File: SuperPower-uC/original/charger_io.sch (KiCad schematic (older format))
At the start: 20 parts, among them J2 Barrel_Jack_Switch, J3 Conn_01x02_Male, Q2 DMP3028LSD, U2 USB-C, U3 IP4220CZ6

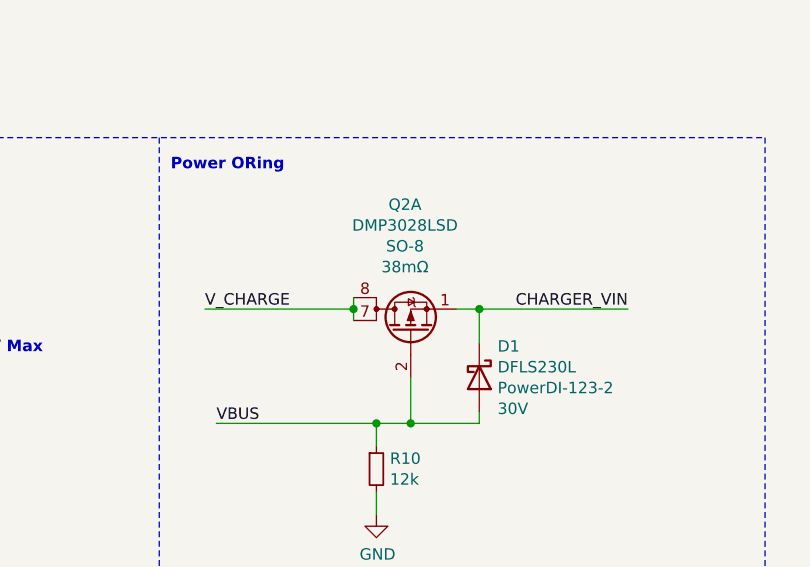
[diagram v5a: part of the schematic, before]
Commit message: Exchanged DMP3028LSD mosfet with Si3421DV
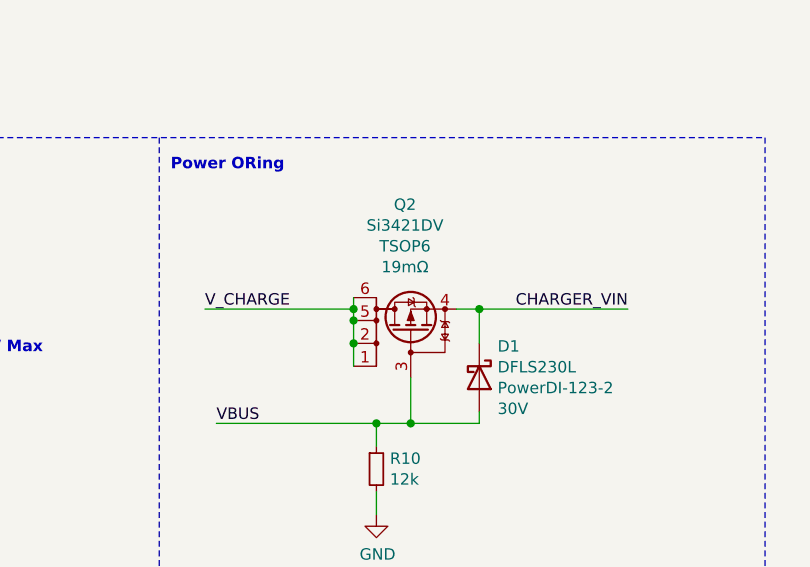
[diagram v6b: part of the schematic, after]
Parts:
- removed Q2: DMP3028LSD, Package_SO:SO-8_3.9x4.9mm_P1.27mm, symbol dmp3028lsd:DMP3028LSD
- added Q2: Si3421DV, Package_SO:TSOP-6_1.65x3.05mm_P0.95mm, symbol dmp2035uvt:DMP2035UVT
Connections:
- net CHARGER_VIN: now also Q2.4 (S)
- net VBUS: now also Q2.3 (G)
- net V_CHARGE: now also Q2.1 (D), Q2.2 (D), Q2.5 (D), Q2.6 (D)
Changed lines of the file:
@@
 Wire Wire Line
 	8600 2850 9250 2850
-$Comp
-L dmp3028lsd:DMP3028LSD Q2
-U 1 1 6007EF0E
-P 9500 2950
-F 0 "Q2" V 10057 2975 50  0000 C CNN
-F 1 "DMP3028LSD" V 9966 2975 50  0000 C CNN
-F 2 "Package_SO:SO-8_3.9x4.9mm_P1.27mm" H 9700 2875 50  0001 L CIN
-F 3 "https://www.diodes.com/assets/Datasheets/DMP3028LSD.pdf" V 9500 2950 50  0001 L CNN
-F 4 "Diodes Incorporated" H 9500 2950 50  0001 C CNN "Mfr_name"
-F 5 "DMP3028LSD-13" H 9500 2950 50  0001 C CNN "Mfr_no"
-F 6 "SO-8" V 9875 2975 50  0000 C CNN "Package"
-F 7 "P + P" H 9500 2950 50  0001 C CNN "mos_Type"
-F 8 "30V" H 9500 2950 50  0001 C CNN "mos_VDSS"
-F 9 "38mΩ" V 9784 2975 50  0000 C CNN "mos_RDSon"
-F 10 "4.7A" H 9500 2950 50  0001 C CNN "mos_IDmax"
-F 11 "1-3V" H 9500 2950 50  0001 C CNN "mos_VGSth"
-F 12 "20V" H 9500 2950 50  0001 C CNN "mos_VGSS"
-F 13 "https://octopart.com/dmp3028lsd-13-diodes+inc.-67250487?r=sp" H 9500 2950 50  0001 C CNN "Octopart_link"
-F 14 "-" H 9500 2950 50  0001 C CNN "Farnell_link"
-F 15 "-" H 9500 2950 50  0001 C CNN "Farnell_ref"
-F 16 "2020-12-05" H 9500 2950 50  0001 C CNN "Farnell_check_date"
-F 17 "-" H 9500 2950 50  0001 C CNN "Farnell_price_qt=1"
-F 18 "-" H 9500 2950 50  0001 C CNN "Farnell_price_qt=10"
-F 19 "-" H 9500 2950 50  0001 C CNN "Farnell_price_qt=100"
-F 20 "-" H 9500 2950 50  0001 C CNN "Farnell_price_qt=1000"
-F 21 "-" H 9500 2950 50  0001 C CNN "Farnell_stock"
-F 22 "https://lcsc.com/product-detail/MOSFET_Diodes-Incorporated-DMP3028LSD-13_C397949.html" H 9500 2950 50  0001 C CNN "LCSC_link"
-F 23 "C397949" H 9500 2950 50  0001 C CNN "LCSC_ref"
-F 24 "2020-12-13" H 9500 2950 50  0001 C CNN "LCSC_check_date"
-F 25 "$0.373" H 9500 2950 50  0001 C CNN "LCSC_price_qt=1"
-F 26 "$0.2802" H 9500 2950 50  0001 C CNN "LCSC_price_qt=10"
-F 27 "$0.2475" H 9500 2950 50  0001 C CNN "LCSC_price_qt=100"
-F 28 "$0.2355" H 9500 2950 50  0001 C CNN "LCSC_price_qt=1000"
-F 29 "4,818" H 9500 2950 50  0001 C CNN "LCSC_stock"
-F 30 "https://www.mouser.fr/ProductDetail/Diodes-Incorporated/DMP3028LSD-13?qs=%2Fha2pyFadugUkRnXWzNfjPB%2F2%2FpUVmcBtenJqlz85NswHo6v693iIw%3D%3D" H 9500 2950 50  0001 C CNN "Mouser_link"
-F 31 "621-DMP3028LSD-13" H 9500 2950 50  0001 C CNN "Mouser_ref"
-F 32 "2020-12-13" H 9500 2950 50  0001 C CNN "Mouser_check_date"
-F 33 "$0.564" H 9500 2950 50  0001 C CNN "Mouser_price_qt=1"
-F 34 "$0.469" H 9500 2950 50  0001 C CNN "Mouser_price_qt=10"
-F 35 "$0.328" H 9500 2950 50  0001 C CNN "Mouser_price_qt=100"
-F 36 "$0.242" H 9500 2950 50  0001 C CNN "Mouser_price_qt=1000"
-F 37 "2,855" H 9500 2950 50  0001 C CNN "Mouser_stock"
-F 38 "-" H 9500 2950 50  0001 C CNN "RS_link"
-F 39 "-" H 9500 2950 50  0001 C CNN "RS_ref"
-F 40 "2020-12-05" H 9500 2950 50  0001 C CNN "RS_check_date"
-F 41 "-" H 9500 2950 50  0001 C CNN "RS_price_qt=1"
-F 42 "-" H 9500 2950 50  0001 C CNN "RS_price_qt=10"
-F 43 "-" H 9500 2950 50  0001 C CNN "RS_price_qt=100"
-F 44 "-" H 9500 2950 50  0001 C CNN "RS_price_qt=1000"
-F 45 "-" H 9500 2950 50  0001 C CNN "RS_stock"
-F 46 "TO_CHECK" H 9500 2950 50  0001 C CNN "Status"
-F 47 "1.03" H 9500 2950 50  0001 C CNN "Release_version"
-F 48 "2020-12-21" H 9500 2950 50  0001 C CNN "Release_date"
-F 49 "ManWithNoName" H 9500 2950 50  0001 C CNN "Designer"
-	1    9500 2950
-	0    -1   -1   0
-$EndComp
 Wire Wire Line
 	8650 3350 9350 3350
@@
 Wire Wire Line
 	9250 2850 9250 2800
+$Comp
+L dmp2035uvt:DMP2035UVT Q?
+U 1 1 6007A550
+P 9500 2950
+AR Path="/5F63A0E9/6007A550" Ref="Q?"  Part="1"
+AR Path="/5F63B107/6007A550" Ref="Q2"  Part="1"
+F 0 "Q2" V 10057 2975 50  0000 C CNN
+F 1 "Si3421DV" V 9966 2975 50  0000 C CNN
+F 2 "Package_SO:TSOP-6_1.65x3.05mm_P0.95mm" H 9700 3050 50  0001 C CNN
+F 3 "https://www.diodes.com/assets/Datasheets/DMP2035UVT.pdf" H 9500 2950 50  0001 C CNN
+F 4 "Diodes Incorporated" H 9500 2950 50  0001 C CNN "Mfr_name"
+F 5 "DMP2035UVT-7" H 9500 2950 50  0001 C CNN "Mfr_no"
+F 6 "TSOP6" V 9875 2975 50  0000 C CNN "Package"
+F 7 "P" H 9500 2950 50  0001 C CNN "mos_Type"
+F 8 "-20V" H 9500 2950 50  0001 C CNN "mos_VDSS"
+F 9 "19mΩ" V 9784 2975 50  0000 C CNN "mos_RDSon"
+F 10 "-6.0A" H 9500 2950 50  0001 C CNN "mos_IDmax"
+F 11 "-0.4V_to_-1.5V" H 9500 2950 50  0001 C CNN "mos_VGSth"
+F 12 "12V" H 9500 2950 50  0001 C CNN "mos_VGSS"
+F 13 "https://octopart.com/dmp2035uvt-7-diodes+inc.-21789379?r=sp" H 9500 2950 50  0001 C CNN "Octopart_link"
+F 14 "https://fr.farnell.com/diodes-inc/dmp2035uvt-7/mosfet-canal-p-20v-6a-150-1-2w/dp/3405183?st=dmp2035uvt" H 9500 2950 50  0001 C CNN "Farnell_link"
+F 15 "3405183" H 9500 2950 50  0001 C CNN "Farnell_ref"
+F 16 "2020-12-11" H 9500 2950 50  0001 C CNN "Farnell_check_date"
+F 17 "-" H 9500 2950 50  0001 C CNN "Farnell_price_qt=1"
+F 18 "0,52 €" H 9500 2950 50  0001 C CNN "Farnell_price_qt=10"
+F 19 "0,238 €" H 9500 2950 50  0001 C CNN "Farnell_price_qt=100"
+F 20 "0,141 €" H 9500 2950 50  0001 C CNN "Farnell_price_qt=1000"
+F 21 "2,890" H 9500 2950 50  0001 C CNN "Farnell_stock"
+F 22 "https://lcsc.com/product-detail/MOSFET_Diodes-Incorporated-DMP2035UVT-7_C260934.html" H 9500 2950 50  0001 C CNN "LCSC_link"
+F 23 "C260934" H 9500 2950 50  0001 C CNN "LCSC_ref"
+F 24 "2020-12-11" H 9500 2950 50  0001 C CNN "LCSC_check_date"
+F 25 "-" H 9500 2950 50  0001 C CNN "LCSC_price_qt=1"
+F 26 "$0.1253" H 9500 2950 50  0001 C CNN "LCSC_price_qt=10"
+F 27 "$0.0932" H 9500 2950 50  0001 C CNN "LCSC_price_qt=100"
+F 28 "$0.0814" H 9500 2950 50  0001 C CNN "LCSC_price_qt=1000"
+F 29 "7,535" H 9500 2950 50  0001 C CNN "LCSC_stock"
+F 30 "https://eu.mouser.com/ProductDetail/Diodes-Incorporated/DMP2035UVT-7?qs=F5djdNSOT4Y3SEHDwWTQ6g%3D%3D" H 9500 2950 50  0001 C CNN "Mouser_link"
+F 31 "621-DMP2035UVT-7" H 9500 2950 50  0001 C CNN "Mouser_ref"
+F 32 "2020-12-11" H 9500 2950 50  0001 C CNN "Mouser_check_date"
+F 33 "$0.474" H 9500 2950 50  0001 C CNN "Mouser_price_qt=1"
+F 34 "$0.346" H 9500 2950 50  0001 C CNN "Mouser_price_qt=10"
+F 35 "$0.215" H 9500 2950 50  0001 C CNN "Mouser_price_qt=100"
+F 36 "$0.137" H 9500 2950 50  0001 C CNN "Mouser_price_qt=1000"
+F 37 "19,684" H 9500 2950 50  0001 C CNN "Mouser_stock"
+F 38 "-" H 9500 2950 50  0001 C CNN "RS_link"
+F 39 "-" H 9500 2950 50  0001 C CNN "RS_ref"
+F 40 "2020-12-11" H 9500 2950 50  0001 C CNN "RS_check_date"
+F 41 "-" H 9500 2950 50  0001 C CNN "RS_price_qt=1"
+F 42 "-" H 9500 2950 50  0001 C CNN "RS_price_qt=10"
+F 43 "-" H 9500 2950 50  0001 C CNN "RS_price_qt=100"
+F 44 "-" H 9500 2950 50  0001 C CNN "RS_price_qt=1000"
+F 45 "-" H 9500 2950 50  0001 C CNN "RS_stock"
+F 46 "TO_CHECK" H 9500 2950 50  0001 C CNN "Status"
+F 47 "1.01" H 9500 2950 50  0001 C CNN "Release_version"
+F 48 "2020-12-18" H 9500 2950 50  0001 C CNN "Release_date"
+F 49 "ManWithNoName" H 9500 2950 50  0001 C CNN "Designer"
+	1    9500 2950
+	0    -1   -1   0
+$EndComp
+Wire Wire Line
+	9250 3100 9250 3000
+Connection ~ 9250 2900
+Connection ~ 9250 3000
+Wire Wire Line
+	9250 3000 9250 2900
 $EndSCHEMATC

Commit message: Exchanged MH with 2.5 + Vias and Pad
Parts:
- H1, H2, H3, H4: footprint MountingHole:MountingHole_2.2mm_M2 -> MountingHole:MountingHole_2.5mm_Pad_Via
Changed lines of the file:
@@
 F 0 "H1" H 1450 2599 50  0000 L CNN
 F 1 "MountingHole_Pad" H 1450 2508 50  0000 L CNN
-F 2 "MountingHole:MountingHole_2.2mm_M2" H 1350 2550 50  0001 C CNN
+F 2 "MountingHole:MountingHole_2.5mm_Pad_Via" H 1350 2550 50  0001 C CNN
 F 3 "~" H 1350 2550 50  0001 C CNN
 	1    1350 2550
@@
 F 0 "H3" H 2350 2599 50  0000 L CNN
 F 1 "MountingHole_Pad" H 2350 2508 50  0000 L CNN
-F 2 "MountingHole:MountingHole_2.2mm_M2" H 2250 2550 50  0001 C CNN
+F 2 "MountingHole:MountingHole_2.5mm_Pad_Via" H 2250 2550 50  0001 C CNN
 F 3 "~" H 2250 2550 50  0001 C CNN
 	1    2250 2550
@@
 F 0 "H2" H 1450 3349 50  0000 L CNN
 F 1 "MountingHole_Pad" H 1450 3258 50  0000 L CNN
-F 2 "MountingHole:MountingHole_2.2mm_M2" H 1350 3300 50  0001 C CNN
+F 2 "MountingHole:MountingHole_2.5mm_Pad_Via" H 1350 3300 50  0001 C CNN
 F 3 "~" H 1350 3300 50  0001 C CNN
 	1    1350 3300
@@
 F 0 "H4" H 2350 3349 50  0000 L CNN
 F 1 "MountingHole_Pad" H 2350 3258 50  0000 L CNN
-F 2 "MountingHole:MountingHole_2.2mm_M2" H 2250 3300 50  0001 C CNN
+F 2 "MountingHole:MountingHole_2.5mm_Pad_Via" H 2250 3300 50  0001 C CNN
 F 3 "~" H 2250 3300 50  0001 C CNN
 	1    2250 3300

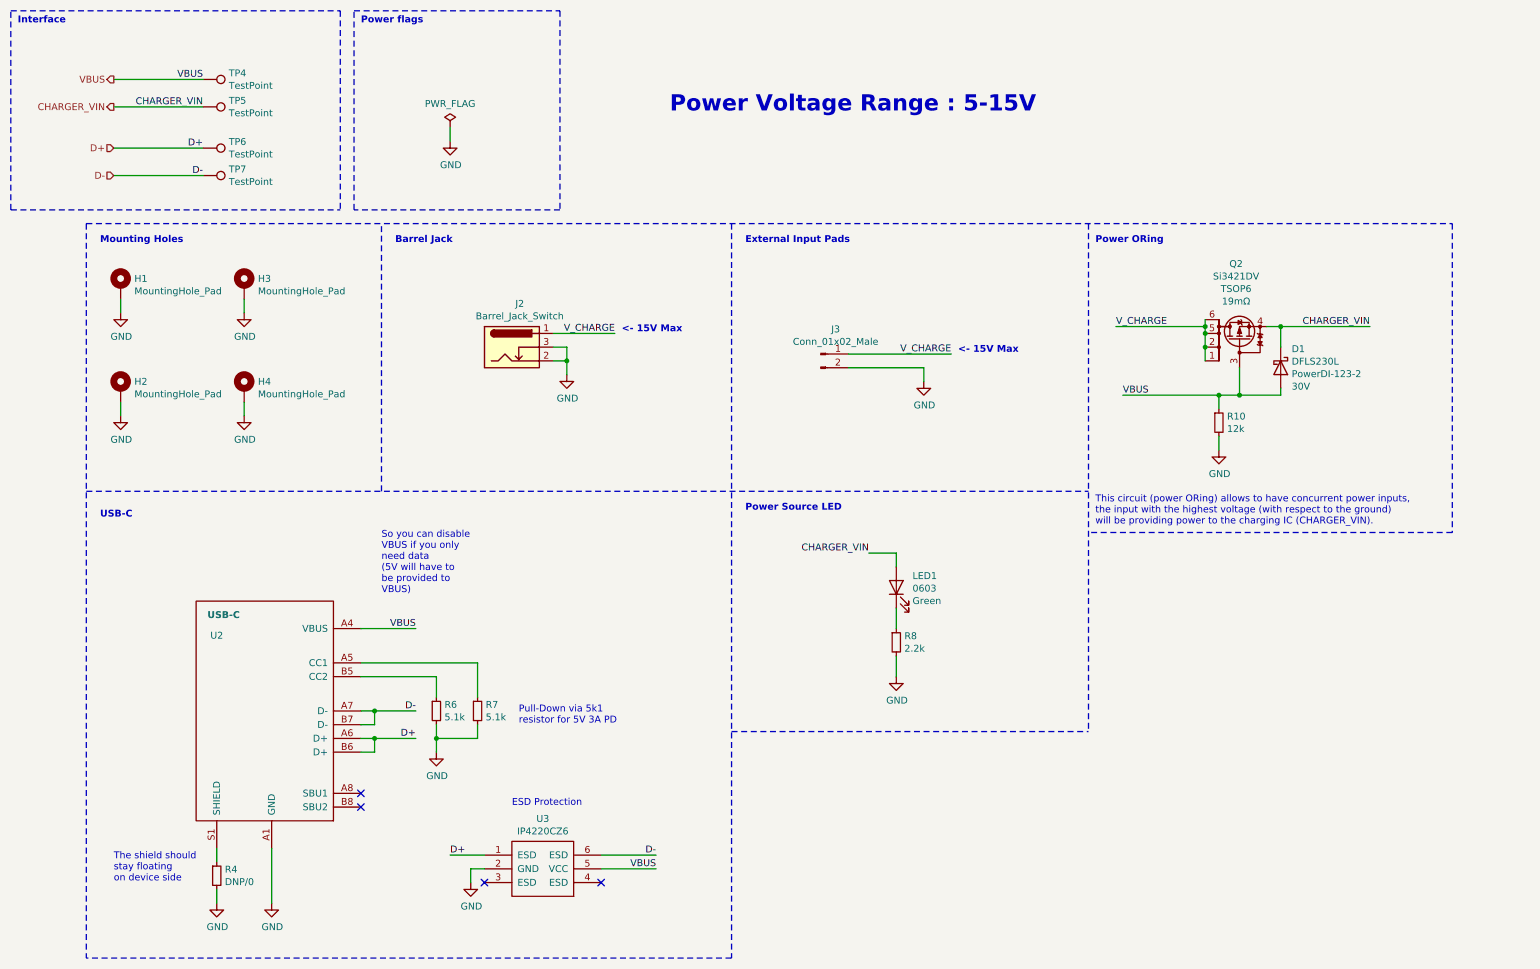
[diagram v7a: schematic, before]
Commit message: Swapped M2.5 with pad to M2.2 without pads
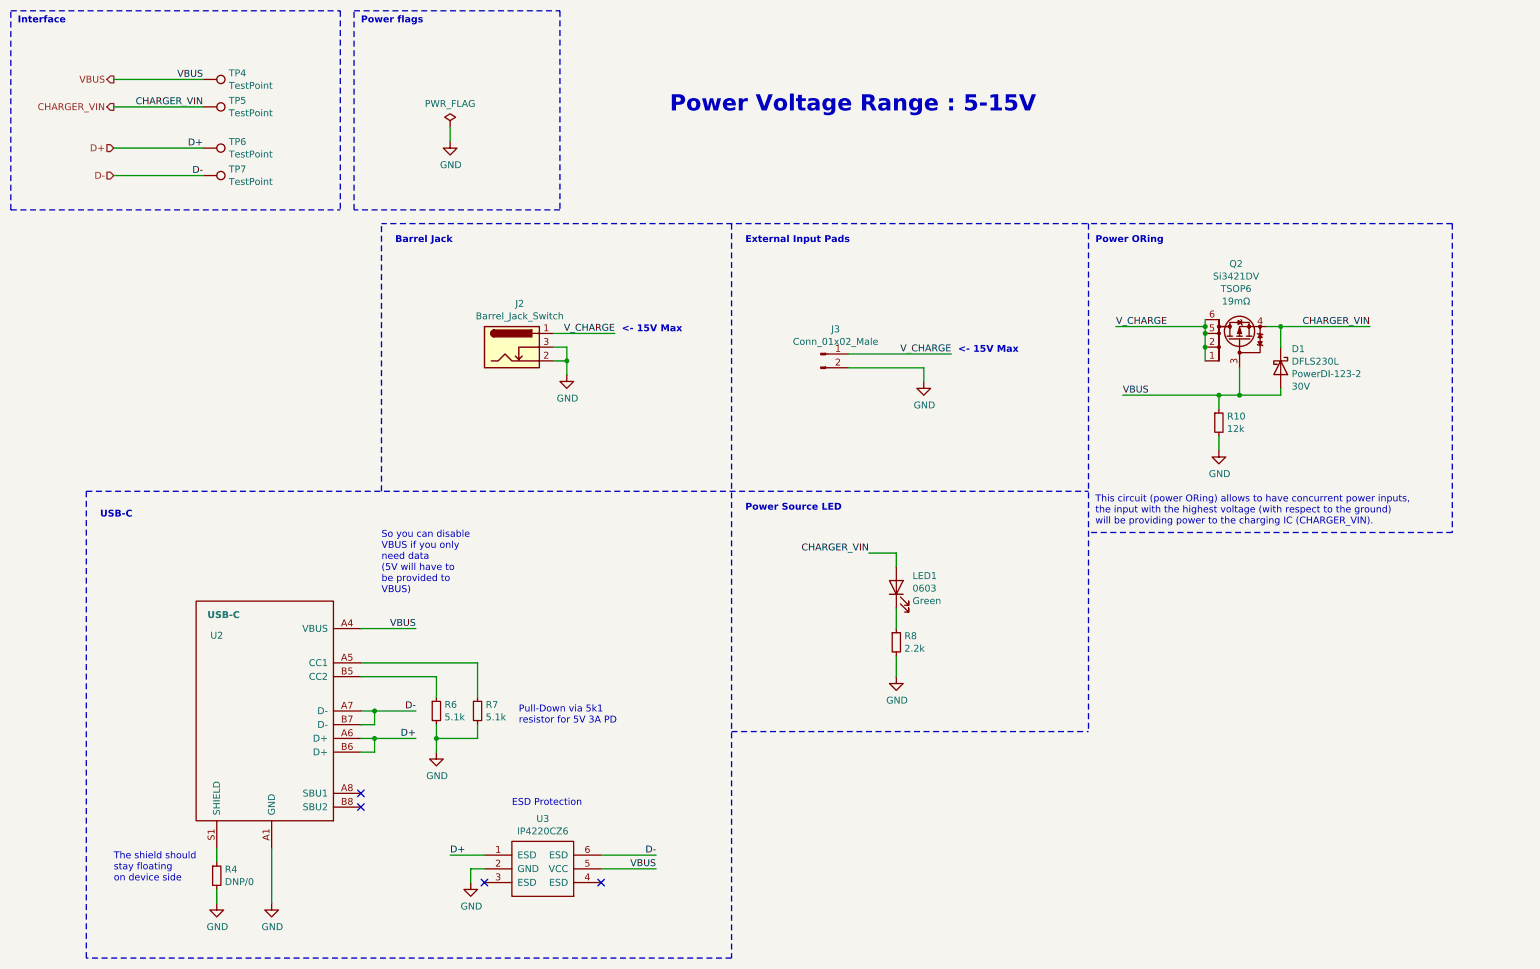
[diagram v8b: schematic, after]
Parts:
- removed H1, H2, H3, H4: MountingHole_Pad, MountingHole:MountingHole_2.5mm_Pad_Via, symbol Mechanical:MountingHole_Pad
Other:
- note removed: "Mounting Holes"
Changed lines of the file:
@@
 Text Notes 7450 3050 0    50   ~ 10
 <- 15V Max
-$Comp
-L Mechanical:MountingHole_Pad H1
-U 1 1 5FDDE91A
-P 1350 2550
-F 0 "H1" H 1450 2599 50  0000 L CNN
-F 1 "MountingHole_Pad" H 1450 2508 50  0000 L CNN
-F 2 "MountingHole:MountingHole_2.5mm_Pad_Via" H 1350 2550 50  0001 C CNN
-F 3 "~" H 1350 2550 50  0001 C CNN
-	1    1350 2550
-	1    0    0    -1
-$EndComp
-$Comp
-L power:GND #PWR010
-U 1 1 5FDE07B4
-P 1350 2750
-F 0 "#PWR010" H 1350 2500 50  0001 C CNN
-F 1 "GND" H 1355 2577 50  0000 C CNN
-F 2 "" H 1350 2750 50  0001 C CNN
-F 3 "" H 1350 2750 50  0001 C CNN
-	1    1350 2750
-	1    0    0    -1
-$EndComp
-Wire Wire Line
-	1350 2750 1350 2650
-Wire Notes Line
-	1100 2100 1100 7450
-Wire Notes Line
-	1100 2100 11050 2100
-Text Notes 1200 2250 0    50   ~ 10
-Mounting Holes
-$Comp
-L Mechanical:MountingHole_Pad H3
-U 1 1 5FDE96CE
-P 2250 2550
-F 0 "H3" H 2350 2599 50  0000 L CNN
-F 1 "MountingHole_Pad" H 2350 2508 50  0000 L CNN
-F 2 "MountingHole:MountingHole_2.5mm_Pad_Via" H 2250 2550 50  0001 C CNN
-F 3 "~" H 2250 2550 50  0001 C CNN
-	1    2250 2550
-	1    0    0    -1
-$EndComp
-$Comp
-L power:GND #PWR013
-U 1 1 5FDE96D4
-P 2250 2750
-F 0 "#PWR013" H 2250 2500 50  0001 C CNN
-F 1 "GND" H 2255 2577 50  0000 C CNN
-F 2 "" H 2250 2750 50  0001 C CNN
-F 3 "" H 2250 2750 50  0001 C CNN
-	1    2250 2750
-	1    0    0    -1
-$EndComp
-Wire Wire Line
-	2250 2750 2250 2650
-$Comp
-L Mechanical:MountingHole_Pad H2
-U 1 1 5FDEB8E4
-P 1350 3300
-F 0 "H2" H 1450 3349 50  0000 L CNN
-F 1 "MountingHole_Pad" H 1450 3258 50  0000 L CNN
-F 2 "MountingHole:MountingHole_2.5mm_Pad_Via" H 1350 3300 50  0001 C CNN
-F 3 "~" H 1350 3300 50  0001 C CNN
-	1    1350 3300
-	1    0    0    -1
-$EndComp
-$Comp
-L power:GND #PWR011
-U 1 1 5FDEB8EA
-P 1350 3500
-F 0 "#PWR011" H 1350 3250 50  0001 C CNN
-F 1 "GND" H 1355 3327 50  0000 C CNN
-F 2 "" H 1350 3500 50  0001 C CNN
-F 3 "" H 1350 3500 50  0001 C CNN
-	1    1350 3500
-	1    0    0    -1
-$EndComp
-Wire Wire Line
-	1350 3500 1350 3400
-$Comp
-L Mechanical:MountingHole_Pad H4
-U 1 1 5FDED307
-P 2250 3300
-F 0 "H4" H 2350 3349 50  0000 L CNN
-F 1 "MountingHole_Pad" H 2350 3258 50  0000 L CNN
-F 2 "MountingHole:MountingHole_2.5mm_Pad_Via" H 2250 3300 50  0001 C CNN
-F 3 "~" H 2250 3300 50  0001 C CNN
-	1    2250 3300
-	1    0    0    -1
-$EndComp
 Wire Wire Line
 	3100 5050 3500 5050
@@
 Wire Wire Line
 	6650 3150 7200 3150
-$Comp
-L power:GND #PWR0105
-U 1 1 5FE15B7B
-P 2250 3500
-F 0 "#PWR0105" H 2250 3250 50  0001 C CNN
-F 1 "GND" H 2255 3327 50  0000 C CNN
-F 2 "" H 2250 3500 50  0001 C CNN
-F 3 "" H 2250 3500 50  0001 C CNN
-	1    2250 3500
-	1    0    0    -1
-$EndComp
-Wire Wire Line
-	2250 3500 2250 3400
 $Comp
 L power:GND #PWR0106
@@
 Wire Wire Line
 	9250 3000 9250 2900
+Wire Notes Line
+	11050 2100 3250 2100
+Wire Notes Line
+	1100 7450 1100 4050
 $EndSCHEMATC
